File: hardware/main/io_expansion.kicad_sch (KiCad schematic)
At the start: 11 parts, among them U9 MPU-6050

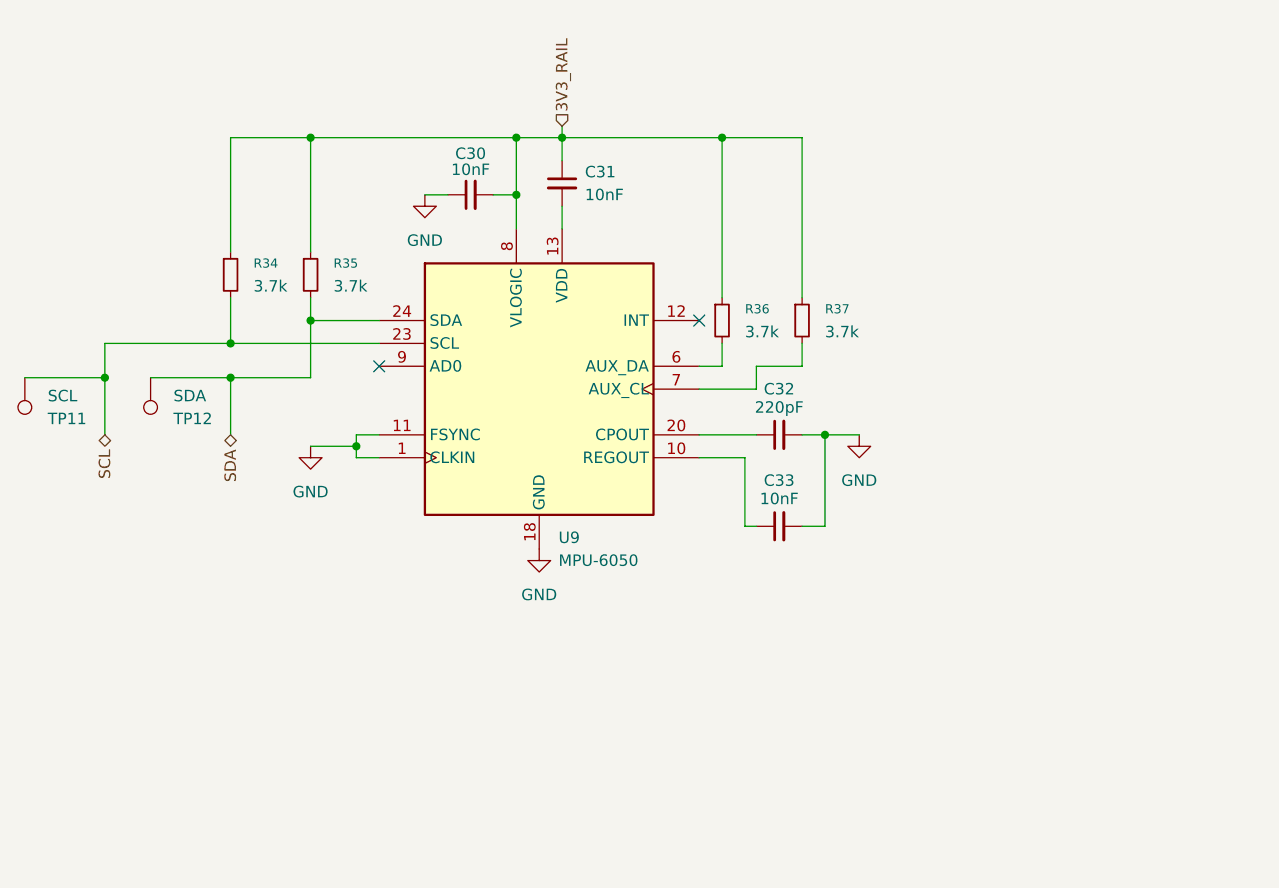
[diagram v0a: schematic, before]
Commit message: expanded main pcb schematics
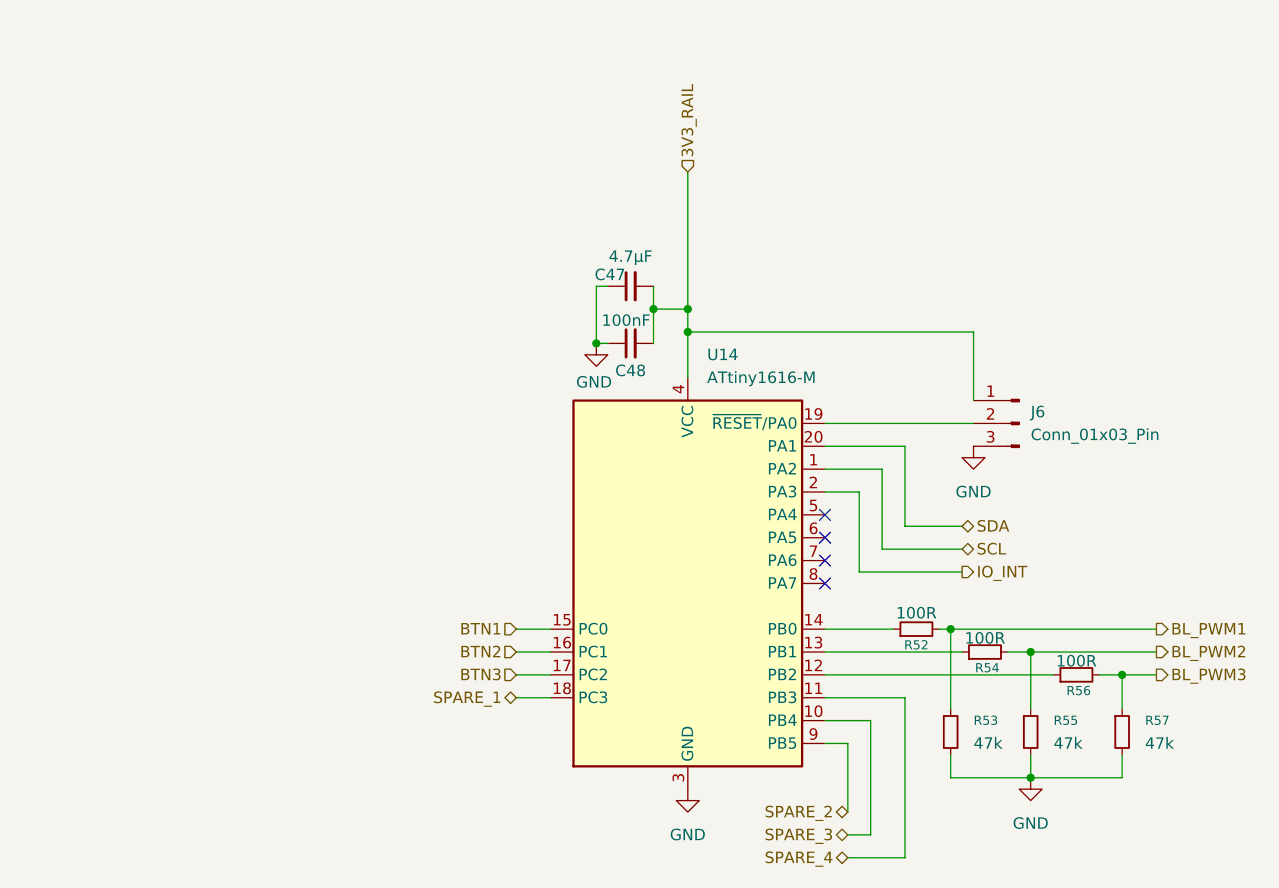
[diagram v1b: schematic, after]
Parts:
- removed C30, C31, C33: 10nF, symbol Device:C_Small
- removed C32: 220pF, symbol Device:C_Small
- removed R34, R35, R36, R37: 3.7k, symbol Device:R_Small
- removed TP11: SCL, symbol Connector:TestPoint
- removed TP12: SDA, symbol Connector:TestPoint
- removed U9: MPU-6050, Sensor_Motion:InvenSense_QFN-24_4x4mm_P0.5mm, symbol Sensor_Motion:MPU-6050
- added C47: 4.7μF, symbol Device:C_Small
- added C48: 100nF, symbol Device:C_Small
- added J6: Conn_01x03_Pin, symbol Connector:Conn_01x03_Pin
- added R52, R54, R56: 100R, symbol Device:R_Small
- added R53, R55, R57: 47k, symbol Device:R_Small
- added U14: ATtiny1616-M, Package_DFN_QFN:VQFN-20-1EP_3x3mm_P0.4mm_EP1.7x1.7mm, symbol MCU_Microchip_ATtiny:ATtiny1616-M
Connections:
- net 3V3_RAIL: now also C47.2, C48.2, J6.1 (Pin_1), U14.4 (VCC)
- net GND: now also C47.1, C48.1, J6.3 (Pin_3), R53.2, R55.2, R57.2, U14.21 (GND), U14.3 (GND)
- net SCL: now also U14.1 (PA2)
- net SDA: now also U14.20 (PA1)
- new net: R56.1, U14.12 (PB2)
- new net: R54.1, U14.13 (PB1)
- new net: R52.1, U14.14 (PB0)
- new net: J6.2 (Pin_2), U14.19 (~{RESET}/PA0)
- new net BL_PWM1: R52.2, R53.1
- new net BL_PWM2: R54.2, R55.1
- new net BL_PWM3: R56.2, R57.1
- new net BTN1: U14.15 (PC0)
- new net BTN2: U14.16 (PC1)
- new net BTN3: U14.17 (PC2)
- new net IO_INT: U14.2 (PA3)
- new net SPARE_1: U14.18 (PC3)
- new net SPARE_2: U14.9 (PB5)
- new net SPARE_3: U14.10 (PB4)
- new net SPARE_4: U14.11 (PB3)
- no-connect marks 2 -> 4
